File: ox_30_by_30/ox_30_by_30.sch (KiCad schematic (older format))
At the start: 22 parts, among them J1 PIX1, J10 R_CONN, J11 PIX1, J12 PIX2, J13 PIX3, J14 BOT_TCE, J16 PIX4, J17 PIX5, J18 PIX6, J19 TCE4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

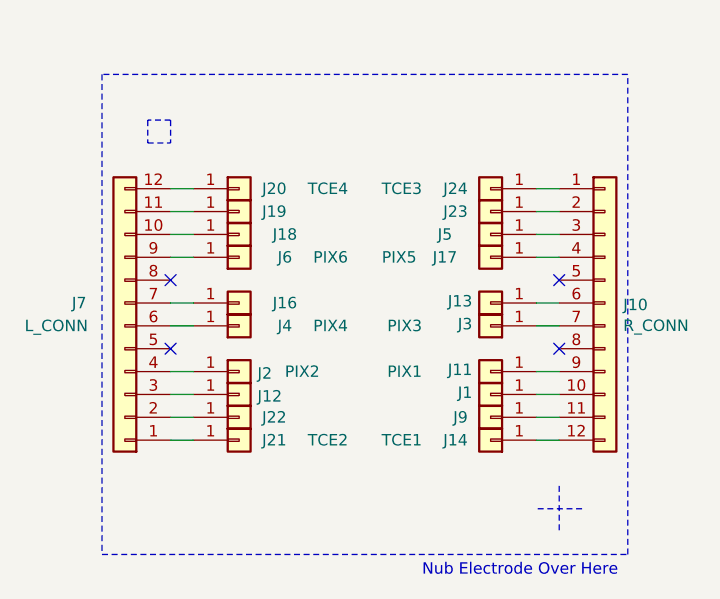
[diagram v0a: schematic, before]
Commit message: lim crossbar pcb done
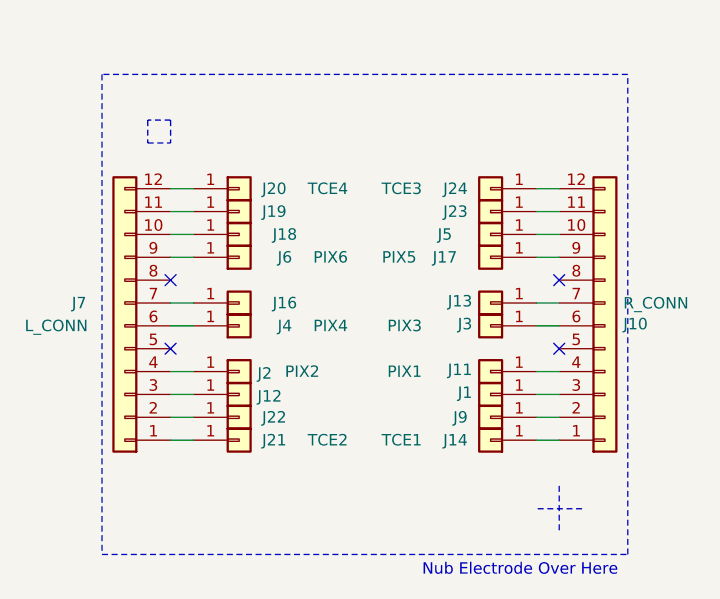
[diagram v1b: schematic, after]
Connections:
- net at J3.1 (Pin_1): now also J10.6 (Pin_6); no longer J10.7 (Pin_7)
- net at J1.1 (Pin_1): now also J10.3 (Pin_3); no longer J10.10 (Pin_10)
- net at J5.1 (Pin_1): now also J10.10 (Pin_10); no longer J10.3 (Pin_3)
- net at J9.1 (Pin_1): now also J10.1 (Pin_1); no longer J10.12 (Pin_12)
- net at J23.1 (Pin_1): now also J10.12 (Pin_12); no longer J10.1 (Pin_1)
- net at J10.11 (Pin_11): now also J24.1 (Pin_1); no longer J14.1 (Pin_1)
- net at J10.2 (Pin_2): now also J14.1 (Pin_1); no longer J24.1 (Pin_1)
- net at J10.4 (Pin_4): now also J11.1 (Pin_1); no longer J17.1 (Pin_1)
- net at J13.1 (Pin_1): now also J10.7 (Pin_7); no longer J10.6 (Pin_6)
- net at J10.9 (Pin_9): now also J17.1 (Pin_1); no longer J11.1 (Pin_1)
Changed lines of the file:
@@
 L Connector_Generic:Conn_01x12 J10
 U 1 1 5DCA2856
-P 6700 3700
-F 0 "J10" H 6780 3692 50  0000 L CNN
-F 1 "R_CONN" H 6780 3601 50  0000 L CNN
-F 2 "Connector_PinHeader_2.00mm:PinHeader_1x12_P2.00mm_Vertical" H 6700 3700 50  0001 C CNN
-F 3 "~" H 6700 3700 50  0001 C CNN
-F 4 "samtec" H 6700 3700 50  0001 C CNN "mfg"
-F 5 "tmm-112-01-g-s" H 6700 3700 50  0001 C CNN "mpn"
-	1    6700 3700
-	1    0    0    -1
+P 6700 3800
+F 0 "J10" H 6780 3792 50  0000 L CNN
+F 1 "R_CONN" H 6780 3701 50  0000 L CNN
+F 2 "Connector_PinHeader_2.00mm:PinHeader_1x12_P2.00mm_Vertical" H 6700 3800 50  0001 C CNN
+F 3 "~" H 6700 3800 50  0001 C CNN
+F 4 "samtec" H 6700 3800 50  0001 C CNN "mfg"
+F 5 "tmm-112-01-g-s" H 6700 3800 50  0001 C CNN "mpn"
+	1    6700 3800
+	1    0    0    1
 $EndComp
 NoConn ~ 4800 3900

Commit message: pre basebord freeroute
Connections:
- net S3: now reaches J10.6 (Pin_6), J3.1 (Pin_1)
- net F2: now reaches J2.1 (Pin_1), J7.4 (Pin_4)
- net S1: now reaches J1.1 (Pin_1), J10.3 (Pin_3)
- net F6: now reaches J6.1 (Pin_1), J7.9 (Pin_9)
- net S5: now reaches J10.10 (Pin_10), J5.1 (Pin_1)
- net S4: now reaches J4.1 (Pin_1), J7.6 (Pin_6)
- net SL1: now reaches J10.1 (Pin_1), J9.1 (Pin_1)
- net FL3: now reaches J10.11 (Pin_11), J24.1 (Pin_1)
- net SL3: now reaches J10.12 (Pin_12), J23.1 (Pin_1)
- net FL1: now reaches J10.2 (Pin_2), J14.1 (Pin_1)
- net F1: now reaches J10.4 (Pin_4), J11.1 (Pin_1)
- net BOT_PHIL: now reaches J10.5 (Pin_5)
- net F3: now reaches J10.7 (Pin_7), J13.1 (Pin_1)
- net F5: now reaches J10.9 (Pin_9), J17.1 (Pin_1)
- net SL2: now reaches J22.1 (Pin_1), J7.1 (Pin_1)
- net S6: now reaches J18.1 (Pin_1), J7.10 (Pin_10)
- net FL4: now reaches J20.1 (Pin_1), J7.11 (Pin_11)
- net SL4: now reaches J19.1 (Pin_1), J7.12 (Pin_12)
- net FL2: now reaches J21.1 (Pin_1), J7.2 (Pin_2)
- net S2: now reaches J12.1 (Pin_1), J7.3 (Pin_3)
- net TOP_PHIL: now reaches J7.5 (Pin_5)
- net F4: now reaches J16.1 (Pin_1), J7.7 (Pin_7)
- no-connect marks 4 -> 2
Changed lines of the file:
@@
 	1    0    0    1
 $EndComp
-NoConn ~ 4800 3900
 NoConn ~ 4800 3600
-NoConn ~ 6500 3600
-NoConn ~ 6500 3900
 Wire Wire Line
 	4800 4100 4900 4100
@@
 Wire Notes Line
 	6800 4800 6800 2700
-Wire Notes Line
-	4500 4800 6800 4800
-Wire Notes Line
-	4500 2700 4500 4800
 Text Notes 5900 4900 0    50   ~ 0
 Nub Electrode Over Here
@@
 Wire Wire Line
 	4800 3300 4900 3300
+Text Label 6400 4300 0    50   ~ 0
+SL1
+Text Label 6400 4200 0    50   ~ 0
+FL1
+Text Label 6400 3200 0    50   ~ 0
+SL3
+Text Label 6400 3300 0    50   ~ 0
+FL3
+Text Label 4800 4300 0    50   ~ 0
+SL2
+Text Label 4800 3300 0    50   ~ 0
+FL4
+Text Label 4800 3200 0    50   ~ 0
+SL4
+Text Label 4800 4200 0    50   ~ 0
+FL2
+Text Label 6400 4100 0    50   ~ 0
+S1
+Text Label 6400 3400 0    50   ~ 0
+S5
+Text Label 4800 3400 0    50   ~ 0
+S6
+Text Label 4800 4100 0    50   ~ 0
+S2
+Text Label 4800 4000 0    50   ~ 0
+F2
+Text Label 4800 3700 0    50   ~ 0
+F4
+Text Label 4800 3800 0    50   ~ 0
+S4
+Text Label 6400 3700 0    50   ~ 0
+F3
+Text Label 6400 3800 0    50   ~ 0
+S3
+Text Label 6400 3500 0    50   ~ 0
+F5
+Text Label 4800 3500 0    50   ~ 0
+F6
+Text Label 6400 4000 0    50   ~ 0
+F1
+Text Label 4900 3900 0    50   ~ 0
+TOP_PHIL
+Wire Notes Line
+	4500 2700 4500 4800
+Wire Notes Line
+	4500 4800 6800 4800
+Text Label 6400 3900 2    50   ~ 0
+BOT_PHIL
+Wire Wire Line
+	4800 3900 4900 3900
+Wire Wire Line
+	6500 3900 6400 3900
+NoConn ~ 6500 3600
 $EndSCHEMATC

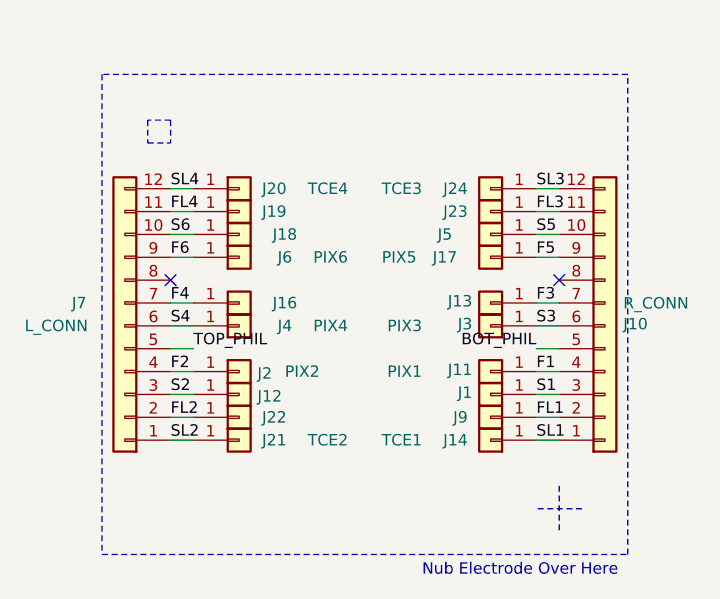
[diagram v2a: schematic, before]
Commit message: add features to oxford adapter
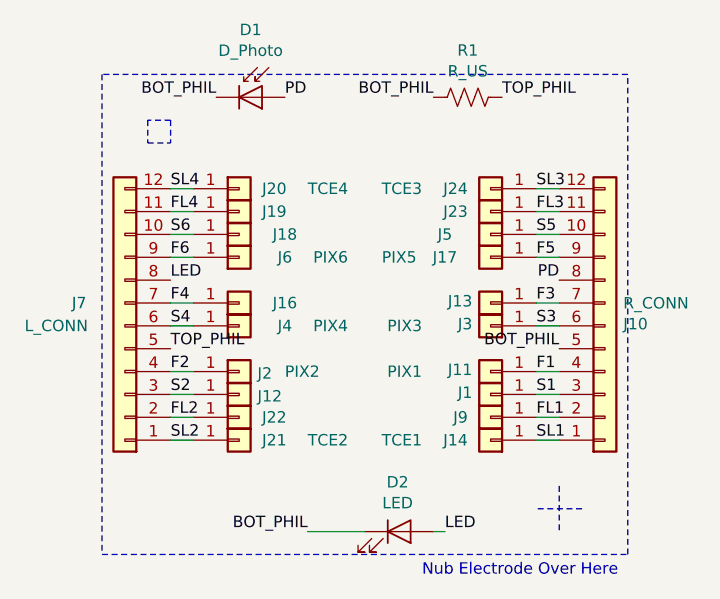
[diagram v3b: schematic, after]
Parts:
- added D1: D_Photo, Diode_SMD:D_0805_2012Metric_Pad1.15x1.40mm_HandSolder, symbol Device:D_Photo
- added D2: LED, LED_SMD:LED_0805_2012Metric_Pad1.15x1.40mm_HandSolder, symbol Device:LED
- added R1: R_US, Resistor_SMD:R_0805_2012Metric_Pad1.15x1.40mm_HandSolder, symbol Device:R_US
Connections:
- net BOT_PHIL: now also D1.1 (K), D2.1 (K), R1.2
- net TOP_PHIL: now also R1.1
- net PD: now reaches J10.8 (Pin_8)
- net PD: now also D1.2 (A)
- net LED: now reaches J7.8 (Pin_8)
- net LED: now also D2.2 (A)
- no-connect marks 2 -> 0
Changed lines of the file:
@@
 	1    0    0    1
 $EndComp
-NoConn ~ 4800 3600
 Wire Wire Line
 	4800 4100 4900 4100
-Wire Wire Line
-	4900 4000 4800 4000
 Wire Wire Line
 	4800 3800 4900 3800
@@
 Text Label 6400 4000 0    50   ~ 0
 F1
-Text Label 4900 3900 0    50   ~ 0
+Text Label 4800 3900 0    50   ~ 0
 TOP_PHIL
 Wire Notes Line
 	4500 2700 4500 4800
+Wire Wire Line
+	4900 4000 4800 4000
+Text Label 6500 3900 2    50   ~ 0
+BOT_PHIL
+$Comp
+L Device:D_Photo D1
+U 1 1 5E21EC8F
+P 5200 2800
+F 0 "D1" H 5150 3095 50  0000 C CNN
+F 1 "D_Photo" H 5150 3004 50  0000 C CNN
+F 2 "Diode_SMD:D_0805_2012Metric_Pad1.15x1.40mm_HandSolder" H 5150 2800 50  0001 C CNN
+F 3 "~" H 5150 2800 50  0001 C CNN
+	1    5200 2800
+	1    0    0    -1
+$EndComp
+Text Label 5000 2800 2    50   ~ 0
+BOT_PHIL
+Text Label 6500 3600 2    50   ~ 0
+PD
+Text Label 5300 2800 0    50   ~ 0
+PD
+Text Label 4800 3600 0    50   ~ 0
+LED
+Text Label 5400 4700 2    50   ~ 0
+BOT_PHIL
+$Comp
+L Device:LED D2
+U 1 1 5E228574
+P 5800 4700
+F 0 "D2" H 5793 4916 50  0000 C CNN
+F 1 "LED" H 5793 4825 50  0000 C CNN
+F 2 "LED_SMD:LED_0805_2012Metric_Pad1.15x1.40mm_HandSolder" H 5800 4700 50  0001 C CNN
+F 3 "~" H 5800 4700 50  0001 C CNN
+	1    5800 4700
+	1    0    0    -1
+$EndComp
+Wire Wire Line
+	5400 4700 5650 4700
 Wire Notes Line
 	4500 4800 6800 4800
-Text Label 6400 3900 2    50   ~ 0
-BOT_PHIL
-Wire Wire Line
-	4800 3900 4900 3900
-Wire Wire Line
-	6500 3900 6400 3900
-NoConn ~ 6500 3600
+Text Label 6000 4700 0    50   ~ 0
+LED
+Wire Wire Line
+	6000 4700 5950 4700
+$Comp
+L Device:R_US R1
+U 1 1 5E23068A
+P 6100 2800
+F 0 "R1" V 5895 2800 50  0000 C CNN
+F 1 "R_US" V 5986 2800 50  0000 C CNN
+F 2 "Resistor_SMD:R_0805_2012Metric_Pad1.15x1.40mm_HandSolder" V 6140 2790 50  0001 C CNN
+F 3 "~" H 6100 2800 50  0001 C CNN
+	1    6100 2800
+	0    1    1    0
+$EndComp
+Text Label 5950 2800 2    50   ~ 0
+BOT_PHIL
+Text Label 6250 2800 0    50   ~ 0
+TOP_PHIL
 $EndSCHEMATC

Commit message: fix lim baseboard bug
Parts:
- J10, J7: mfg samtec -> harwin; mpn tmm-112-01-g-s -> M22-2511205
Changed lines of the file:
@@
 F 2 "Connector_PinHeader_2.00mm:PinHeader_1x12_P2.00mm_Vertical" H 4600 3800 50  0001 C CNN
 F 3 "~" H 4600 3800 50  0001 C CNN
-F 4 "samtec" H 4600 3800 50  0001 C CNN "mfg"
-F 5 "tmm-112-01-g-s" H 4600 3800 50  0001 C CNN "mpn"
+F 4 "harwin" H 4600 3800 50  0001 C CNN "mfg"
+F 5 "M22-2511205" H 4600 3800 50  0001 C CNN "mpn"
 	1    4600 3800
 	-1   0    0    1
@@
 F 2 "Connector_PinHeader_2.00mm:PinHeader_1x12_P2.00mm_Vertical" H 6700 3800 50  0001 C CNN
 F 3 "~" H 6700 3800 50  0001 C CNN
-F 4 "samtec" H 6700 3800 50  0001 C CNN "mfg"
-F 5 "tmm-112-01-g-s" H 6700 3800 50  0001 C CNN "mpn"
+F 4 "harwin" H 6700 3800 50  0001 C CNN "mfg"
+F 5 "M22-2511205" H 6700 3800 50  0001 C CNN "mpn"
 	1    6700 3800
 	1    0    0    1
